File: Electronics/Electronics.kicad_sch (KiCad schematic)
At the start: 10 parts, among them K1 G3MB-202P, K2 G3MB-202P, K3 G3MB-202P, K4 G3MB-202P, U1 PC817, U2 PC817, U3 PC817, U4 PC817, U5 CH340N

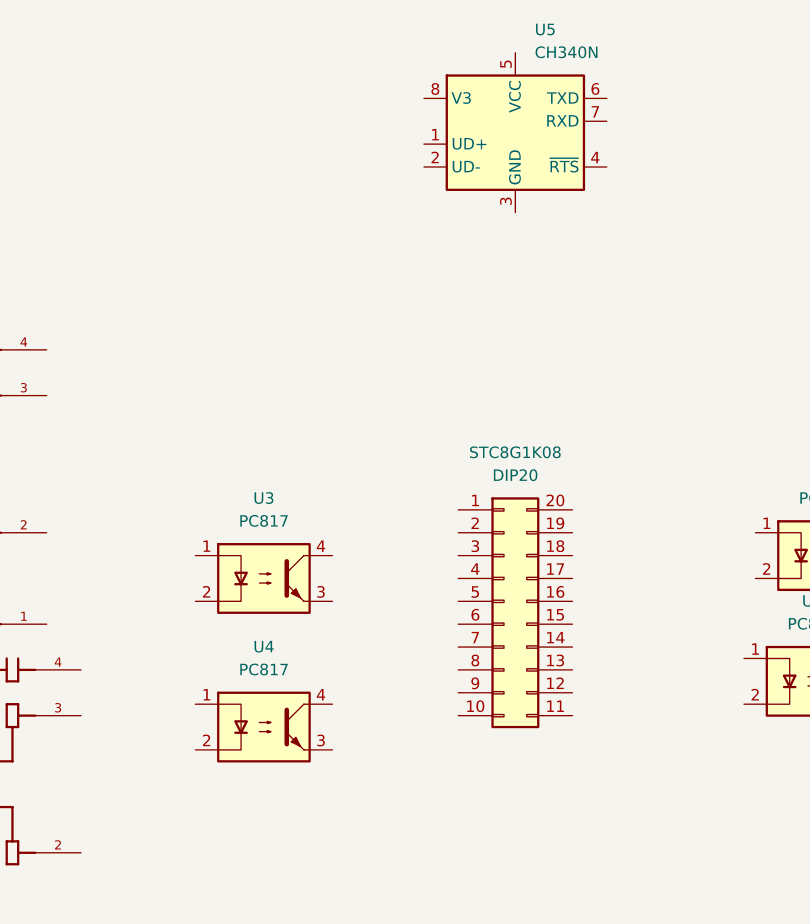
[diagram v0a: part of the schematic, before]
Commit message: finished STC Microcontroller Code structure and most init functions
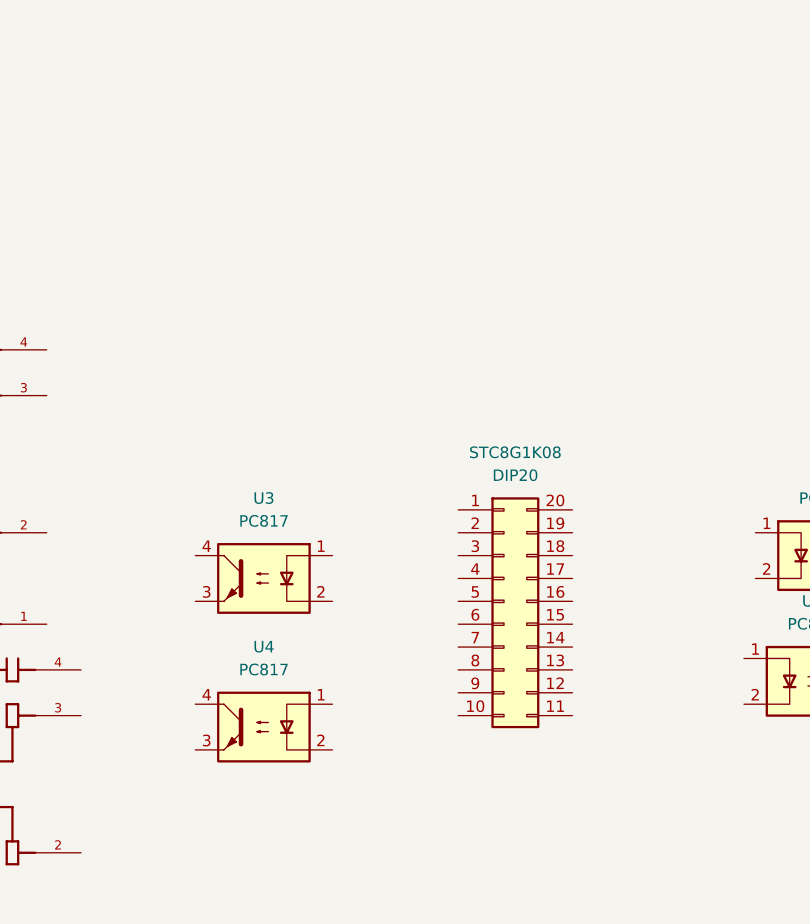
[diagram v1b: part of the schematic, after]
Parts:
- removed U5: CH340N, Package_SO:SOP-8_3.9x4.9mm_P1.27mm, symbol Interface_USB:CH340N
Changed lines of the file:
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@@
-	)
-	(symbol
-		(lib_id "Interface_USB:CH340N")
-		(at 132.08 54.61 0)
-		(unit 1)
-		(exclude_from_sim no)
-		(in_bom yes)
-		(on_board yes)
-		(dnp no)
-		(fields_autoplaced yes)
-		(property "Reference" "U5"
-			(at 134.2233 44.45 0)
-			(effects
-				(font
-					(size 1.27 1.27)
-				)
-				(justify left)
-			)
-		)
-		(property "Value" "CH340N"
-			(at 134.2233 46.99 0)
-			(effects
-				(font
-					(size 1.27 1.27)
-				)
-				(justify left)
-			)
-		)
-		(property "Footprint" "Package_SO:SOP-8_3.9x4.9mm_P1.27mm"
-			(at 128.27 35.56 0)
-			(effects
-				(font
-					(size 1.27 1.27)
-				)
-				(hide yes)
-			)
-		)
-		(property "Datasheet" "https://aitendo3.sakura.ne.jp/aitendo_data/product_img/ic/inteface/CH340N/ch340n.pdf"
-			(at 129.54 49.53 0)
-			(effects
-				(font
-					(size 1.27 1.27)
-				)
-				(hide yes)
-			)
-		)
-		(property "Description" "USB serial converter, 2Mbps, UART, SOP-8"
-			(at 132.08 54.61 0)
-			(effects
-				(font
-					(size 1.27 1.27)
-				)
-				(hide yes)
-			)
-		)
-		(pin "2"
-		)
-		(pin "1"
-		)
-		(pin "7"
-		)
-		(pin "5"
-		)
-		(pin "4"
-		)
-		(pin "6"
-		)
-		(pin "3"
-		)
-		(pin "8"
-		)
-		(instances
-			(project ""
-				(path "/bbb11482-ea5f-48ec-b0d1-73802744c455"
-					(reference "U5")
-					(unit 1)
-				)
-			)
-		)
 	)
 	(symbol
@@
 		(lib_id "Isolator:PC817")
 		(at 104.14 121.92 0)
+		(mirror y)
 		(unit 1)
 		(exclude_from_sim no)
@@
 		)
 		(property "Footprint" "Package_DIP:DIP-4_W7.62mm"
-			(at 99.06 127 0)
+			(at 109.22 127 0)
 			(effects
 				(font
@@
 		(lib_id "Isolator:PC817")
 		(at 104.14 105.41 0)
+		(mirror y)
 		(unit 1)
 		(exclude_from_sim no)
@@
 		)
 		(property "Footprint" "Package_DIP:DIP-4_W7.62mm"
-			(at 99.06 110.49 0)
-			(effects
-				(font
+			(at 109.22 110.49 0)
+			(effects
+				(font

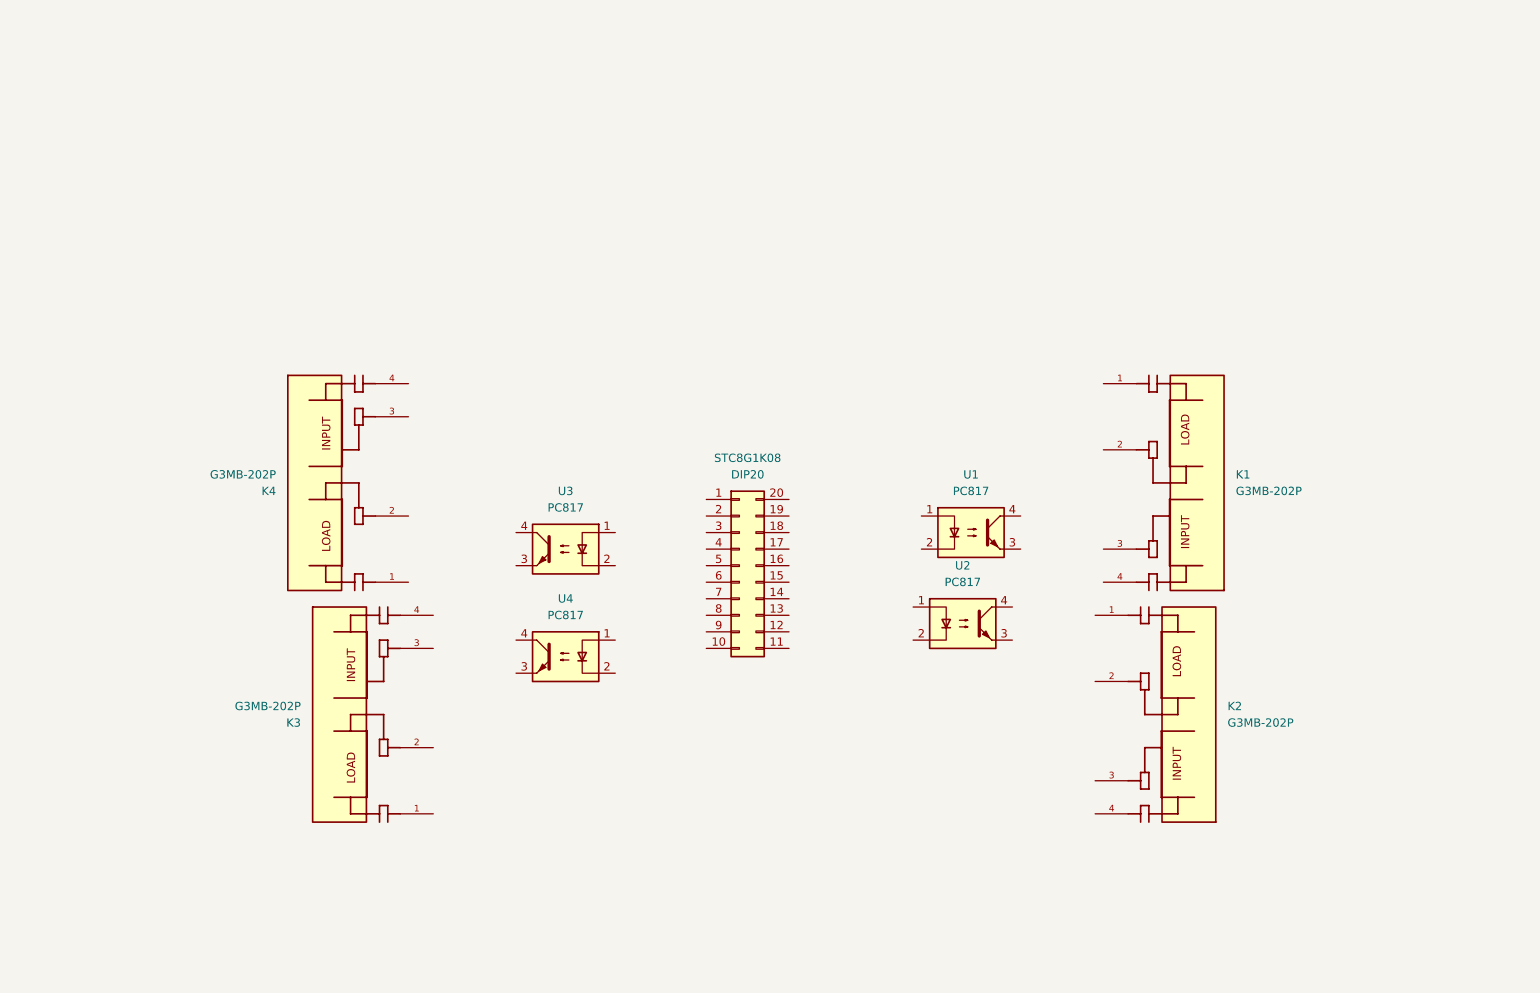
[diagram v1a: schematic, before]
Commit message: finished circuit schematic, pin assignment, added inits of ws2812 PRGB LED
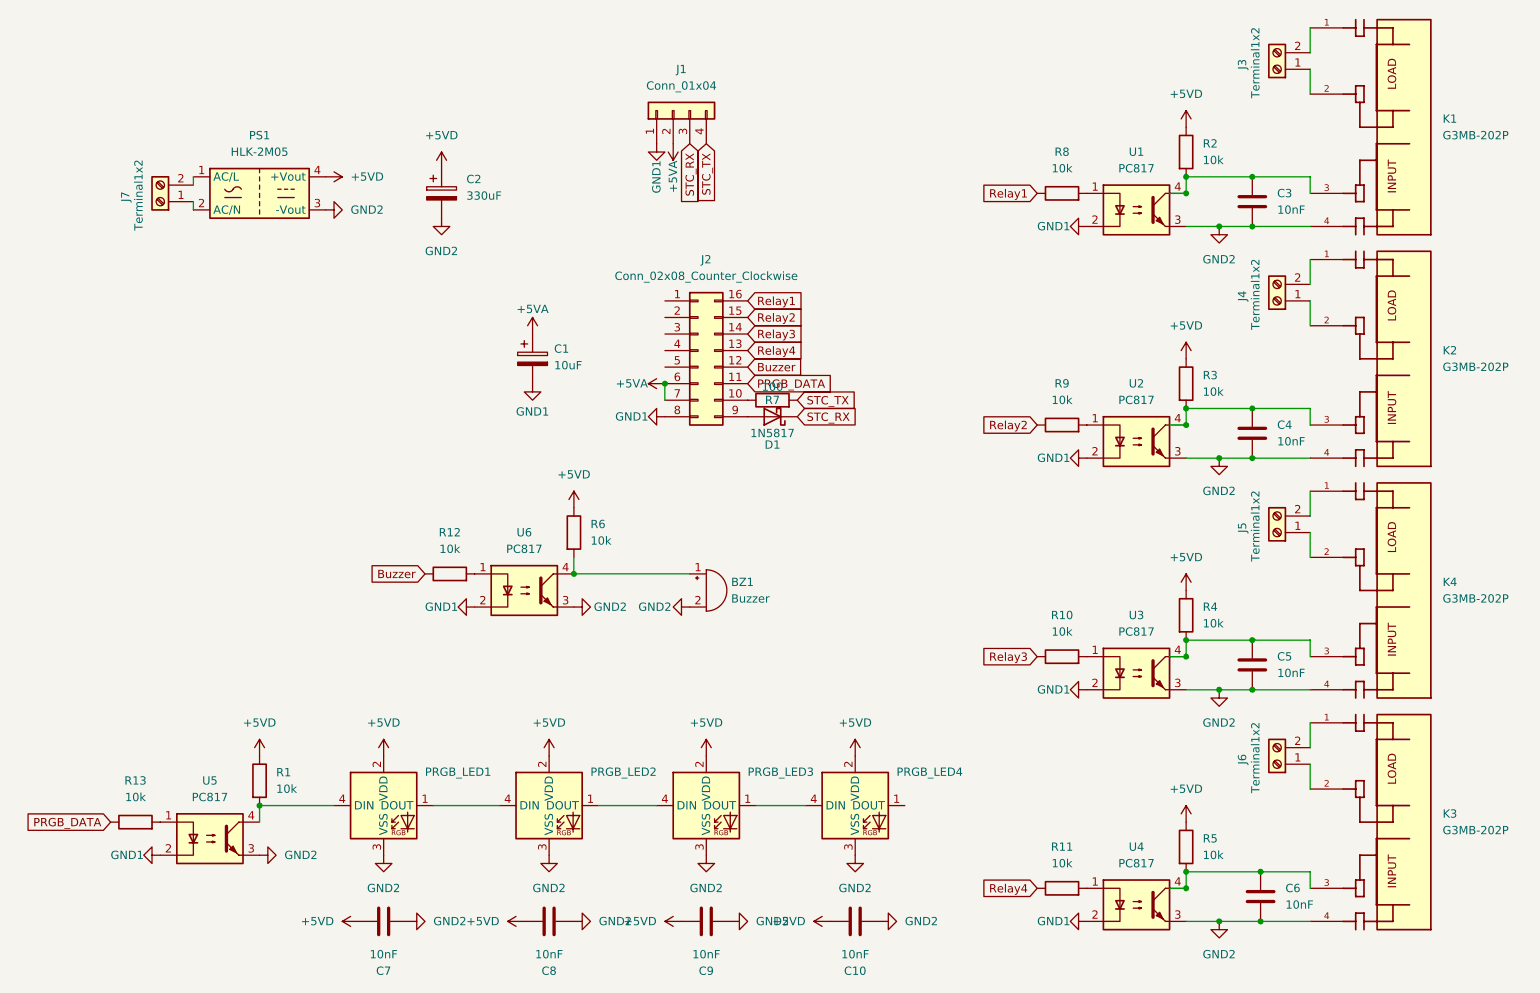
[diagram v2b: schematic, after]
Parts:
- removed STC8G1K08: DIP20, Package_DIP:DIP-20_W7.62mm_LongPads, symbol Connector_Generic:Conn_02x10_Counter_Clockwise
- added BZ1: Buzzer, Buzzer_Beeper:Buzzer_TDK_PS1240P02BT_D12.2mm_H6.5mm, symbol Device:Buzzer
- added C1: 10uF, Capacitor_THT:CP_Radial_D5.0mm_P2.50mm, symbol Device:C_Polarized
- added C10, C3, C4, C5, C6, C7, C8, C9: 10nF, Capacitor_THT:C_Disc_D5.0mm_W2.5mm_P2.50mm, symbol Device:C
- added C2: 330uF, Capacitor_THT:CP_Radial_D6.3mm_P2.50mm, symbol Device:C_Polarized
- added D1: 1N5817, Diode_THT:D_DO-41_SOD81_P7.62mm_Horizontal, symbol Diode:1N5817
- added J1: Conn_01x04, Connector_JST:JST_EH_S4B-EH_1x04_P2.50mm_Horizontal, symbol Connector_Generic:Conn_01x04
- added J2: Conn_02x08_Counter_Clockwise, Package_SO:STC_SOP-16_3.9x9.9mm_P1.27mm, symbol Connector_Generic:Conn_02x08_Counter_Clockwise
- added J3, J4, J5, J6, J7: Terminal1x2, TerminalBlock:TerminalBlock_bornier-2_P5.08mm, symbol Connector:Screw_Terminal_01x02
- added PRGB_LED1, PRGB_LED2, PRGB_LED3, PRGB_LED4: ~, WS2812D-F5:PRGB_LED_DIP_Wide, symbol WS2812D-F5:WS2812D-F5
- added PS1: HLK-2M05, Converter_ACDC:Converter_ACDC_Hi-Link_HLK-2Mxx, symbol Converter_ACDC:HLK-2M05
- added R1, R10, R11, R12, R13, R2, R3, R4, R5, R6, R8, R9: 10k, Resistor_THT:R_Axial_DIN0207_L6.3mm_D2.5mm_P7.62mm_Horizontal, symbol Device:R
- added R7: 100, Resistor_THT:R_Axial_DIN0207_L6.3mm_D2.5mm_P7.62mm_Horizontal, symbol Device:R
- added U5, U6: PC817, Package_DIP:DIP-4_W7.62mm, symbol Isolator:PC817
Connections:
- net at U2.1: now also R9.2
- net GND1: now reaches U2.2
- net GND1: now also U1.2, U3.2, U4.2, C1.2, J1.1 (Pin_1), J2.8 (Pin_8), U5.2, U6.2
- net GND2: now reaches U2.3
- net GND2: now also K1.4, K2.4, K3.4, K4.4, U1.3, U3.3, U4.3, BZ1.2 (-), C10.1, C2.2, C3.2, C4.2, C5.2, C6.2, C7.1, C8.1, C9.1, PRGB_LED1.3 (VSS), PRGB_LED2.3 (VSS), PRGB_LED3.3 (VSS), PRGB_LED4.3 (VSS), PS1.3 (-Vout), U5.3, U6.3
- net at U2.4: now also K2.3, C4.1, R3.2
- net at K3.1: now also J6.2 (Pin_2)
- net at K3.2: now also J6.1 (Pin_1)
- net at K3.3: now also U4.4, C6.1, R5.2
- net at K4.1: now also J5.2 (Pin_2)
- net at K4.2: now also J5.1 (Pin_1)
- net at K4.3: now also U3.4, C5.1, R4.2
- net at K1.1: now also J3.2 (Pin_2)
- net at K1.2: now also J3.1 (Pin_1)
- net at K1.3: now also U1.4, C3.1, R2.2
- net at U4.1: now also R11.2
- net at K2.1: now also J4.2 (Pin_2)
- net at K2.2: now also J4.1 (Pin_1)
- net at U3.1: now also R10.2
- net at U1.1: now also R8.2
- new net: PRGB_LED1.1 (DOUT), PRGB_LED2.4 (DIN)
- new net: PRGB_LED1.4 (DIN), R1.2, U5.4
- new net: R13.2, U5.1
- new net: BZ1.1 (+), R6.2, U6.4
- new net: PRGB_LED3.1 (DOUT), PRGB_LED4.4 (DIN)
- new net: J2.10 (Pin_10), R7.1
- new net: PRGB_LED2.1 (DOUT), PRGB_LED3.4 (DIN)
- new net: J7.2 (Pin_2), PS1.1 (AC/L)
- new net: J7.1 (Pin_1), PS1.2 (AC/N)
- new net: D1.2 (A), J2.9 (Pin_9)
- new net: R12.2, U6.1
- new net +5VA: C1.1, J1.2 (Pin_2), J2.6 (Pin_6), J2.7 (Pin_7)
- new net +5VD: C10.2, C2.1, C7.2, C8.2, C9.2, PRGB_LED1.2 (VDD), PRGB_LED2.2 (VDD), PRGB_LED3.2 (VDD), PRGB_LED4.2 (VDD), PS1.4 (+Vout), R1.1, R2.1, R3.1, R4.1, R5.1, R6.1
- new net Buzzer: J2.12 (Pin_12), R12.1
- new net PRGB_DATA: J2.11 (Pin_11), R13.1
- new net Relay1: J2.16 (Pin_16), R8.1
- new net Relay2: J2.15 (Pin_15), R9.1
- new net Relay3: J2.14 (Pin_14), R10.1
- new net Relay4: J2.13 (Pin_13), R11.1
- new net STC_RX: D1.1 (K), J1.3 (Pin_3)
- new net STC_TX: J1.4 (Pin_4), R7.2
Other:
- moved on the sheet: K1, K2, K3, K4, U1, U2, U3, U4

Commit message: finished C implementation of Relay Control
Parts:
- R10, R11, R8, R9: value 10k -> 1k
- R2, R3, R4, R5: value 10k -> 470
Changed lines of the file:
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@@
 			)
 		)
-		(property "Value" "10k"
+		(property "Value" "1k"
 			(at 180.34 118.11 90)
 			(effects
@@
 			)
 		)
-		(property "Value" "10k"
+		(property "Value" "470"
 			(at 201.93 45.7199 0)
 			(effects
@@
 			)
 		)
-		(property "Value" "10k"
+		(property "Value" "470"
 			(at 201.93 116.8399 0)
 			(effects
@@
 			)
 		)
-		(property "Value" "10k"
+		(property "Value" "1k"
 			(at 180.34 46.99 90)
 			(effects
@@
 			)
 		)
-		(property "Value" "10k"
+		(property "Value" "470"
 			(at 201.93 152.3999 0)
 			(effects
@@
 			)
 		)
-		(property "Value" "10k"
+		(property "Value" "1k"
 			(at 180.34 82.55 90)
 			(effects
@@
 			)
 		)
-		(property "Value" "10k"
+		(property "Value" "470"
 			(at 201.93 81.2799 0)
 			(effects
@@
 			)
 		)
-		(property "Value" "10k"
+		(property "Value" "1k"
 			(at 180.34 153.67 90)
 			(effects

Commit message: finished PCB layout
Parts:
- removed PS1: HLK-2M05, Converter_ACDC:Converter_ACDC_Hi-Link_HLK-2Mxx, symbol Converter_ACDC:HLK-2M05
- added H1, H2, H3: MountingHole, MountingHole:MountingHole_2.7mm_Pad, symbol Mechanical:MountingHole
- added PS1: HLK-5M05, Converter_ACDC:Converter_ACDC_Hi-Link_HLK-5Mxx, symbol Converter_ACDC:HLK-5M05
- CP2102_TTL_Converter1: renamed from J1; value Conn_01x04 -> PinHeader1x4; footprint Connector_JST:JST_EH_S4B-EH_1x04_P2.50mm_Horizontal -> Connector_PinSocket_2.54mm:PinSocket_1x04_P2.54mm_Vertical
- R1: value 10k -> 75
- R10, R11, R8, R9: value 1k -> 330
- R12: value 10k -> 1k
- R13, R6: value 10k -> 220
- STC8H8K64U1: renamed from J2; value Conn_02x08_Counter_Clockwise -> SOP16_Breakout; footprint Package_SO:STC_SOP-16_3.9x9.9mm_P1.27mm -> Module:Pololu_Breakout-16_15.2x20.3mm
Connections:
- net +5VA: no longer STC8H8K64U1.7 (Pin_7)
- net +5VD: now also PS1.4 (+Vout)
- net Buzzer: now also STC8H8K64U1.15 (Pin_15); no longer STC8H8K64U1.12 (Pin_12)
- net GND2: now also PS1.3 (-Vout)
- net PRGB_DATA: now also STC8H8K64U1.16 (Pin_16); no longer STC8H8K64U1.11 (Pin_11)
- net Relay1: now also STC8H8K64U1.11 (Pin_11); no longer STC8H8K64U1.16 (Pin_16)
- net Relay2: now also STC8H8K64U1.12 (Pin_12); no longer STC8H8K64U1.15 (Pin_15)
- net at J7.2 (Pin_2): now also PS1.1 (AC/L)
- net at J7.1 (Pin_1): now also PS1.2 (AC/N)
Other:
- moved on the sheet: BZ1, C10, C7, C8, C9, CP2102_TTL_Converter1, PRGB_LED1, PRGB_LED2, PRGB_LED3, PRGB_LED4, R1, R12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

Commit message: added a force anchor hole for the PCB
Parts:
- added H4: MountingHole, MountingHole:MountingHole_2.7mm_Pad, symbol Mechanical:MountingHole
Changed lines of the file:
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@@
+	)
+	(symbol
+		(lib_id "Mechanical:MountingHole")
+		(at 49.53 85.09 0)
+		(unit 1)
+		(exclude_from_sim no)
+		(in_bom no)
+		(on_board yes)
+		(dnp no)
+		(fields_autoplaced yes)
+		(property "Reference" "H4"
+			(at 52.07 83.8199 0)
+			(effects
+				(font
+					(size 1.27 1.27)
+				)
+				(justify left)
+			)
+		)
+		(property "Value" "MountingHole"
+			(at 52.07 86.3599 0)
+			(effects
+				(font
+					(size 1.27 1.27)
+				)
+				(justify left)
+			)
+		)
+		(property "Footprint" "MountingHole:MountingHole_2.7mm_Pad"
+			(at 49.53 85.09 0)
+			(effects
+				(font
+					(size 1.27 1.27)
+				)
+				(hide yes)
+			)
+		)
+		(property "Datasheet" "~"
+			(at 49.53 85.09 0)
+			(effects
+				(font
+					(size 1.27 1.27)
+				)
+				(hide yes)
+			)
+		)
+		(property "Description" "Mounting Hole without connection"
+			(at 49.53 85.09 0)
+			(effects
+				(font
+					(size 1.27 1.27)
+				)
+				(hide yes)
+			)
+		)
+		(instances
+			(project "Electronics"
+				(path "/bbb11482-ea5f-48ec-b0d1-73802744c455"
+					(reference "H4")
+					(unit 1)
+				)
+			)
+		)
 	)
 	(symbol
